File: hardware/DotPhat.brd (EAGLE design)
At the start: 30 x 65 mm, 57 parts, among them CN1 1X4-BIG, IC1 CAT24M010TS, IC3 SI1145, J3 USB-MICROB, Q1 BSH103, U1 ATMEGA328P-MU-QFN32, U2 TMP102, U3 ATSHA204-TSU, X2 MC-RTC-RV-4162-C7-I2C, X3 S4B-ZR

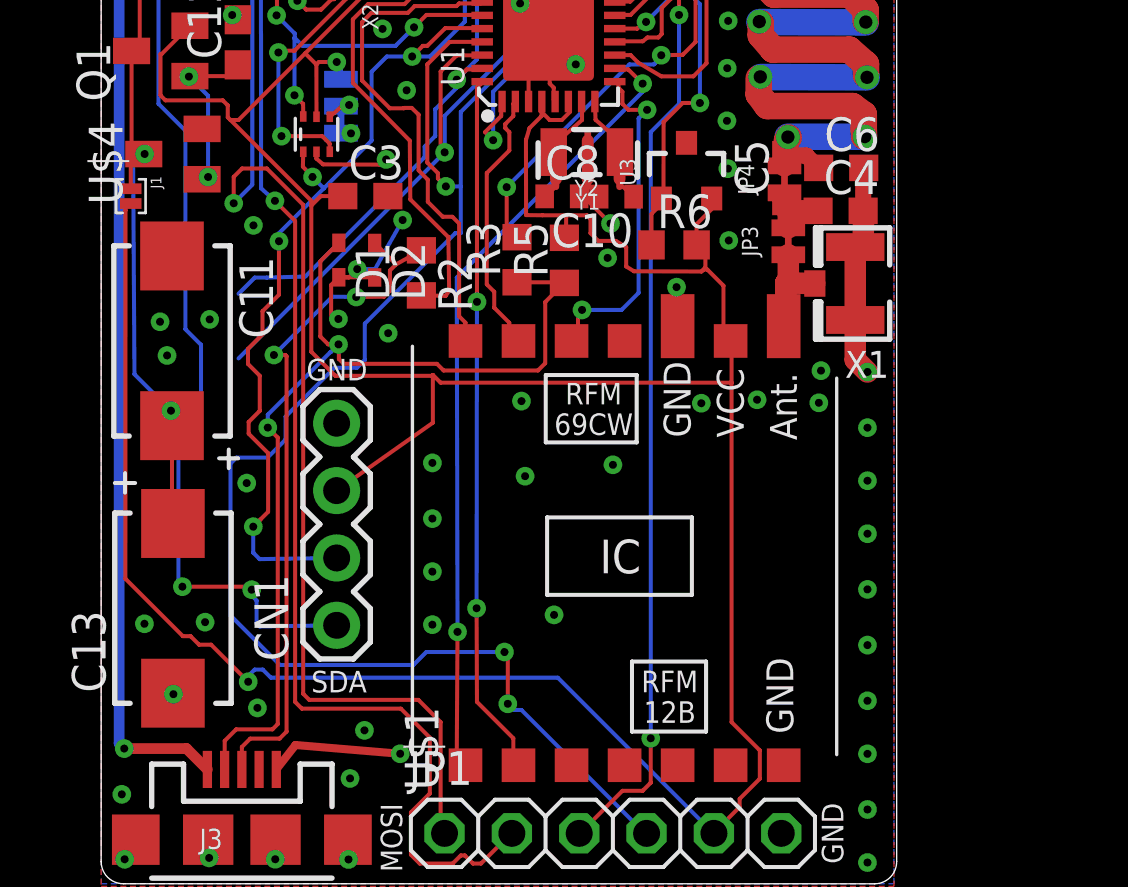
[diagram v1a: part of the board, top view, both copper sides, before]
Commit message: Move caps from parallel to series
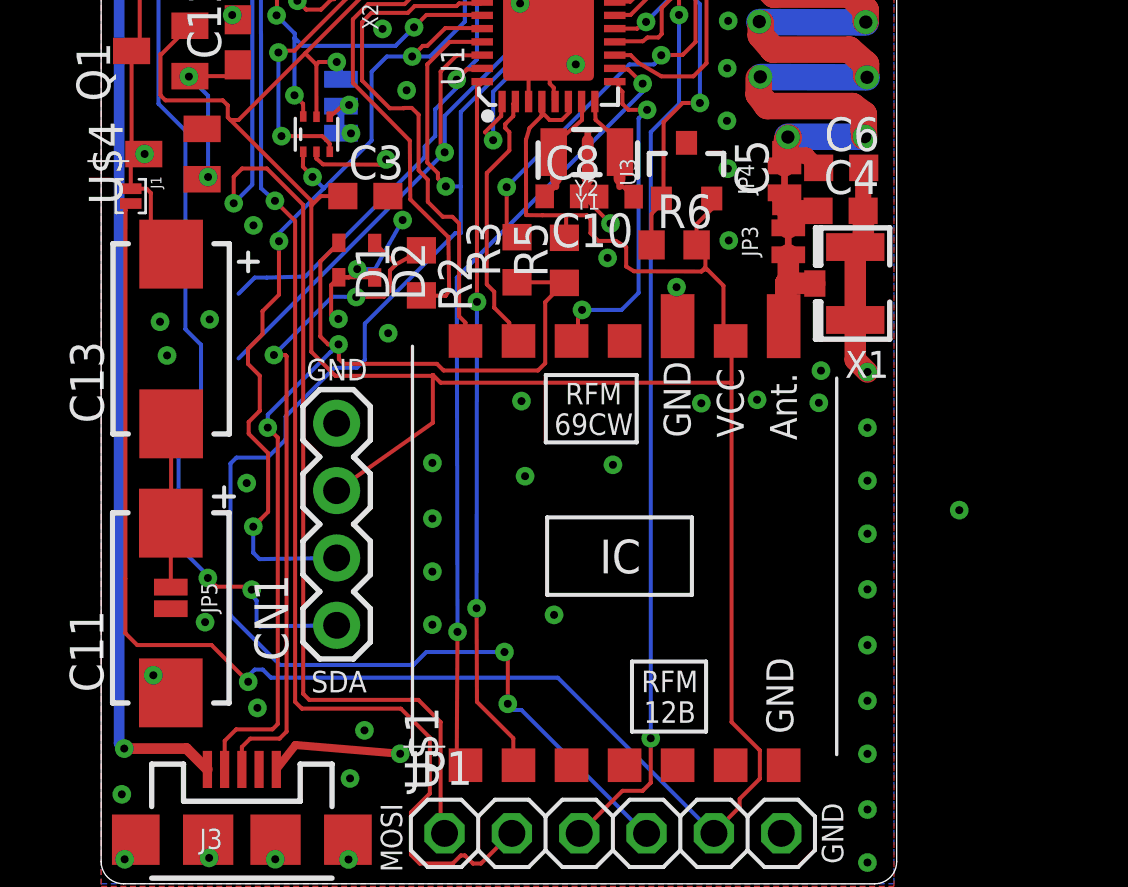
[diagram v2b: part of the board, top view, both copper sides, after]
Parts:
- added JP5: JUMPER-SMT_2_NO_NO-SILK, SparkFun-Jumpers:SMT-JUMPER_2_NO_NO-SILK
- moved C13 10.2 mm to (2.64, 20.5)
- moved C11 10.1 mm to (2.63, 10.4), turned to 90 degrees
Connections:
- new net N$25: C11.+, C13.-, JP5.1
- net CAPS_VCC: no longer C11.+
- net GND: now also JP5.2; no longer C13.-
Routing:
- net CAPS_VCC: track 27.2 -> 16.4 mm, vias 2 -> 1
- net N$25: track 0.00 -> 6.17 mm
- net +3V3: track 234.3 -> 235.5 mm
- net SDA: track 100.6 -> 99.9 mm
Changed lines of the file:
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@@
 <circle x="3.516" y="33.564" radius="0.146453125" width="0.1524" layer="21"/>
 <circle x="3.557" y="33.546" radius="0.055971875" width="0.1524" layer="21"/>
-<wire x1="4.448" y1="16.045" x2="5.171" y2="16.045" width="0.1524" layer="21"/>
-<wire x1="4.813" y1="16.376" x2="4.813" y2="15.67" width="0.1524" layer="21"/>
-<wire x1="0.516" y1="15.113" x2="1.282" y2="15.113" width="0.1524" layer="21"/>
-<wire x1="0.901" y1="15.486" x2="0.901" y2="14.752" width="0.1524" layer="21"/>
+<wire x1="5.189" y1="23.457" x2="5.912" y2="23.457" width="0.1524" layer="21"/>
+<wire x1="5.545" y1="23.805" x2="5.545" y2="23.099" width="0.1524" layer="21"/>
+<wire x1="4.245" y1="14.604" x2="5.011" y2="14.604" width="0.1524" layer="21"/>
+<wire x1="4.638" y1="14.953" x2="4.638" y2="14.219" width="0.1524" layer="21"/>
 </plain>
 <attributes>
@@
 <element name="D3" library="SparkFun" package="SOLARBIT-12X1" value="Solar Cell 4V" x="3.837" y="47.45" rot="R90"/>
 <element name="D4" library="diode" package="SOD523" value="3.6V Zener" x="1.455" y="34.564" rot="R90"/>
-<element name="C11" library="adafruit" package="CT7343" value="1500uF 4V" x="2.672" y="20.476" rot="R270"/>
-<element name="C13" library="adafruit" package="CT7343" value="1500uF 4V" x="2.707" y="10.387" rot="R90"/>
+<element name="C11" library="adafruit" package="CT7343" value="1500uF 4V" x="2.627" y="10.399" rot="R90"/>
+<element name="C13" library="adafruit" package="CT7343" value="1500uF 4V" x="2.639" y="20.545" rot="R90"/>
 <element name="D5" library="diode" package="SOD523" value="0.3V Schottky" x="4.296" y="34.56" rot="R90"/>
 <element name="Q1" library="adafruit" package="SOT23" value="BSH103" x="2.247" y="31.408" rot="R90"/>
@@
 <element name="TP1" library="SparkFun" package="PAD.03X.03" value="TEST-POINT3" x="16.006" y="40.157"/>
 <element name="J1" library="solderjumper" package="2.MED" value="" x="1.117" y="25.933" rot="R270"/>
+<element name="JP5" library="SparkFun-Jumpers" package="SMT-JUMPER_2_NO_NO-SILK" value="JUMPER-SMT_2_NO_NO-SILK" x="2.627" y="10.78" rot="R270"/>
 </elements>
 <signals>
@@
 <via x="13.3812" y="42.225" extent="1-16" drill="0.3"/>
 <contactref element="D3" pad="-"/>
-<contactref element="C11" pad="-"/>
-<contactref element="C13" pad="-"/>
 <contactref element="D4" pad="A"/>
 <wire x1="1.13365625" y1="63.929865625" x2="1.6" y2="64.396209375" width="0.1524" layer="16"/>
@@
 <via x="5.489240625" y="15.109725" extent="1-16" drill="0.3"/>
 <via x="5.743240625" y="24.828725" extent="1-16" drill="0.3"/>
-<via x="2.725240625" y="7.148725" extent="1-16" drill="0.3"/>
-<via x="1.632240625" y="9.803725" extent="1-16" drill="0.3"/>
+<via x="32.362240625" y="14.089725" extent="1-16" drill="0.3"/>
+<via x="1.967240625" y="7.861725" extent="1-16" drill="0.3"/>
 <via x="3.920240625" y="9.865725" extent="1-16" drill="0.3"/>
 <via x="2.927859375" y="53.956615625" extent="1-16" drill="0.3"/>
@@
 <via x="11.480859375" y="53.973615625" extent="1-16" drill="0.3"/>
 <via x="14.073859375" y="48.023615625" extent="1-16" drill="0.3"/>
+<contactref element="C11" pad="-"/>
+<contactref element="JP5" pad="2"/>
+<wire x1="28.9" y1="13.2" x2="32.362240625" y2="14.089725" width="0" layer="19" extent="1-1"/>
 </signal>
 <signal name="SDA">
@@
 <via x="5.678" y="11.09" extent="1-16" drill="0.3"/>
 <wire x1="5.678" y1="11.09" x2="5.565" y2="11.203" width="0.1524" layer="1"/>
-<wire x1="5.565" y1="11.203" x2="3.064" y2="11.203" width="0.1524" layer="1"/>
-<via x="3.064" y="11.203" extent="1-16" drill="0.3"/>
-<wire x1="3.064" y1="11.203" x2="2.912" y2="11.355" width="0.1524" layer="16"/>
-<wire x1="2.912" y1="11.355" x2="2.912" y2="16.649" width="0.1524" layer="16"/>
+<via x="4.024" y="11.53" extent="1-16" drill="0.3"/>
 <wire x1="2.912" y1="16.649" x2="3.766" y2="17.503" width="0.1524" layer="16"/>
 <wire x1="3.766" y1="17.503" x2="3.766" y2="20.326" width="0.1524" layer="16"/>
@@
 <wire x1="7.602684375" y1="54.939" x2="7.504684375" y2="55.037" width="0.1524" layer="16"/>
 <wire x1="6.63" y1="33.753" x2="6.63" y2="32.765" width="0.1524" layer="1"/>
+<wire x1="5.565" y1="11.203" x2="4.351" y2="11.203" width="0.1524" layer="1"/>
+<wire x1="4.351" y1="11.203" x2="4.024" y2="11.53" width="0.1524" layer="1"/>
+<wire x1="4.024" y1="11.53" x2="4.024" y2="11.621" width="0.1524" layer="16"/>
+<wire x1="4.024" y1="11.621" x2="2.921" y2="12.724" width="0.1524" layer="16"/>
+<wire x1="2.921" y1="12.724" x2="2.921" y2="16.64" width="0.1524" layer="16"/>
+<wire x1="2.921" y1="16.64" x2="2.912" y2="16.649" width="0.1524" layer="16"/>
 </signal>
 <signal name="RST">
@@
 <wire x1="1.117" y1="25.6536" x2="1.117" y2="25.595" width="0.1524" layer="1"/>
 <wire x1="0.919" y1="25.397" x2="0.913" y2="11.505" width="0.1524" layer="1"/>
-<wire x1="0.913" y1="11.505" x2="3.081" y2="9.337" width="0.1524" layer="1"/>
-<wire x1="3.081" y1="9.337" x2="3.371" y2="9.337" width="0.1524" layer="1"/>
-<wire x1="3.371" y1="9.337" x2="3.692" y2="9.016" width="0.1524" layer="1"/>
-<wire x1="3.692" y1="9.016" x2="4.147" y2="9.016" width="0.1524" layer="1"/>
-<wire x1="4.147" y1="9.016" x2="5.545" y2="7.618" width="0.1524" layer="1"/>
 <via x="5.545" y="7.618" extent="1-16" drill="0.3"/>
 <wire x1="5.545" y1="7.618" x2="5.545" y2="7.831" width="0.1524" layer="16"/>
@@
 <wire x1="0.919" y1="25.397" x2="0.919" y2="25.6536" width="0.1524" layer="1"/>
 <wire x1="0.919" y1="25.6536" x2="1.117" y2="25.6536" width="0.1524" layer="1"/>
+<wire x1="0.913" y1="11.505" x2="0.913" y2="9.448" width="0.1524" layer="1"/>
+<wire x1="0.913" y1="9.448" x2="1.359" y2="9.002" width="0.1524" layer="1"/>
+<wire x1="1.359" y1="9.002" x2="4.161" y2="9.002" width="0.1524" layer="1"/>
+<wire x1="4.161" y1="9.002" x2="5.545" y2="7.618" width="0.1524" layer="1"/>
 <wire x1="9.26490625" y1="59.71336875" x2="9.6006" y2="59.71" width="0" layer="19" extent="1-1"/>
 </signal>
@@
 </signal>
 <signal name="CAPS_VCC">
-<contactref element="C13" pad="+"/>
-<contactref element="C11" pad="+"/>
 <contactref element="U$4" pad="3"/>
 <contactref element="D5" pad="C"/>
@@
 <wire x1="1.639" y1="27.522" x2="1.475" y2="27.522" width="0.1524" layer="16"/>
 <wire x1="1.475" y1="27.522" x2="1.206" y2="27.253" width="0.1524" layer="16"/>
-<wire x1="1.206" y1="27.253" x2="1.256" y2="19.217" width="0.1524" layer="16"/>
-<wire x1="1.256" y1="19.217" x2="2.633" y2="17.84" width="0.1524" layer="16"/>
-<via x="2.633" y="17.84" extent="1-16" drill="0.3"/>
-<wire x1="2.633" y1="17.84" x2="2.633" y2="17.315" width="0.1524" layer="1"/>
-<wire x1="2.633" y1="17.315" x2="2.672" y2="17.276" width="0.1524" layer="1"/>
-<wire x1="2.672" y1="17.276" x2="2.672" y2="13.622" width="0.1524" layer="1"/>
-<wire x1="2.672" y1="13.622" x2="2.707" y2="13.587" width="0.1524" layer="1"/>
 <contactref element="J1" pad="1"/>
 <wire x1="1.117" y1="26.2124" x2="1.117" y2="27.522" width="0.1524" layer="1"/>
 <wire x1="1.117" y1="27.522" x2="1.639" y2="27.522" width="0.1524" layer="1"/>
+<contactref element="C13" pad="+"/>
+<wire x1="2.658" y1="23.764" x2="2.639" y2="23.745" width="0.1524" layer="1"/>
+<wire x1="1.117" y1="26.2124" x2="1.7126" y2="26.2124" width="0.1524" layer="1"/>
+<wire x1="1.7126" y1="26.2124" x2="1.873" y2="26.052" width="0.1524" layer="1"/>
+<wire x1="1.873" y1="26.052" x2="1.873" y2="24.511" width="0.1524" layer="1"/>
+<wire x1="1.873" y1="24.511" x2="2.639" y2="23.745" width="0.1524" layer="1"/>
 </signal>
 <signal name="MOSFET">
@@
 <contactref element="IC3" pad="4"/>
 </signal>
+<signal name="N$25">
+<contactref element="C11" pad="+"/>
+<contactref element="C13" pad="-"/>
+<wire x1="2.627" y1="13.599" x2="2.639" y2="13.599" width="0.1524" layer="1"/>
+<wire x1="2.639" y1="13.599" x2="2.639" y2="17.345" width="0.1524" layer="1"/>
+<contactref element="JP5" pad="1"/>
+<wire x1="2.627" y1="11.1864" x2="2.627" y2="13.599" width="0.1524" layer="1"/>
+</signal>
 </signals>

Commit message: Irrelevant since will be reverted
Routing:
- net GND: vias 145 -> 144
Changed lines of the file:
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@@
 <via x="5.489240625" y="15.109725" extent="1-16" drill="0.3"/>
 <via x="5.743240625" y="24.828725" extent="1-16" drill="0.3"/>
-<via x="32.362240625" y="14.089725" extent="1-16" drill="0.3"/>
 <via x="1.967240625" y="7.861725" extent="1-16" drill="0.3"/>
 <via x="3.920240625" y="9.865725" extent="1-16" drill="0.3"/>
@@
 <contactref element="C11" pad="-"/>
 <contactref element="JP5" pad="2"/>
-<wire x1="28.9" y1="13.2" x2="32.362240625" y2="14.089725" width="0" layer="19" extent="1-1"/>
 </signal>
 <signal name="SDA">

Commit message: Revert "Irrelevant since will be reverted"
This reverts commit e891d672a37a9ace9540b21aee4dc257b77b94d6.
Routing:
- net GND: vias 144 -> 145
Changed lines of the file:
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@@
 <via x="5.489240625" y="15.109725" extent="1-16" drill="0.3"/>
 <via x="5.743240625" y="24.828725" extent="1-16" drill="0.3"/>
+<via x="32.362240625" y="14.089725" extent="1-16" drill="0.3"/>
 <via x="1.967240625" y="7.861725" extent="1-16" drill="0.3"/>
 <via x="3.920240625" y="9.865725" extent="1-16" drill="0.3"/>
@@
 <contactref element="C11" pad="-"/>
 <contactref element="JP5" pad="2"/>
+<wire x1="28.9" y1="13.2" x2="32.362240625" y2="14.089725" width="0" layer="19" extent="1-1"/>
 </signal>
 <signal name="SDA">
